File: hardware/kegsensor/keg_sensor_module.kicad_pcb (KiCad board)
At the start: 2 copper layers, 155 x 90 mm, 7 parts, among them J1 TerminalBlock_bornier-3_P5.08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, J2 TerminalBlock_bornier-3_P5.08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, J3 TerminalBlock_bornier-3_P5.08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, J4 TerminalBlock_bornier-3_P5.08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, J5 PinSocket_1x04_P2.54mm_Vertic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, J6 PinSocket_1x04_P2.54mm_Vertic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, J7 RJ14_Connfly_DS1133-S4_Horizo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

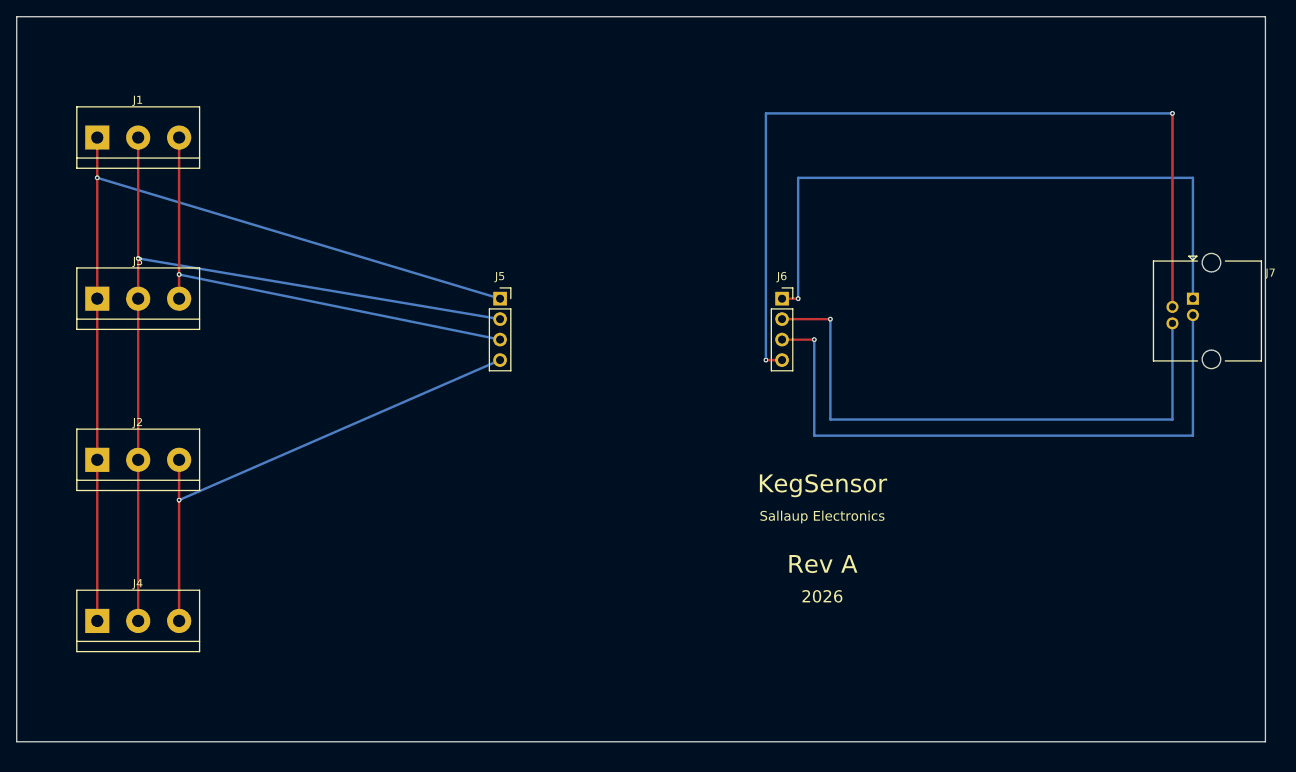
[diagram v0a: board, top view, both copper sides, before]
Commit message: Move KegSensor's J1-J4 sensor terminals to a horizontal row near the top edge
Previously a vertical column near the left edge. Rotated each terminal
block -90deg so its 3 pins stack in Y instead of spreading in X - without
that, all 4 parts' pins would land on identical y-values and the
EXC_POS/EXC_NEG/SIG_POS/SIG_NEG buses couldn't cross the row without
shorting. Rerouted the J1-J4<->J5 bus accordingly; went through a couple
of DRC-guided rounds after straight diagonals cut through unrelated pads
(J2's own pad, then J5's adjacent pad) and an existing J6<->J7 GND trace
that now ran too close to J4's new position.

Also fixed a latent bug the multi-instance footprint copies exposed:
generate_pcb.py kept each copied footprint's nested pad/graphic UUIDs
verbatim from the library file, so J1/J3/J2/J4 (all the same footprint)
shared identical pad UUIDs and confused DRC's violation reporting. Now
re-rolls every nested UUID per instance.

Case updated to match: the J1-J4 wire-exit cutout moved from the left
wall to the front wall, so the engraved branding (which lived there)
moved to the back wall instead, reusing the already-implemented
wall_text_back() - re-verified correct via a mirrored 2D cross-section
from the actual outside-viewer's perspective.

ERC clean, DRC 0 errors (only pre-existing accepted warnings remain),
both case STLs still Simple: yes.

Co-Authored-By: Claude Sonnet 5 <noreply@anthropic.com>
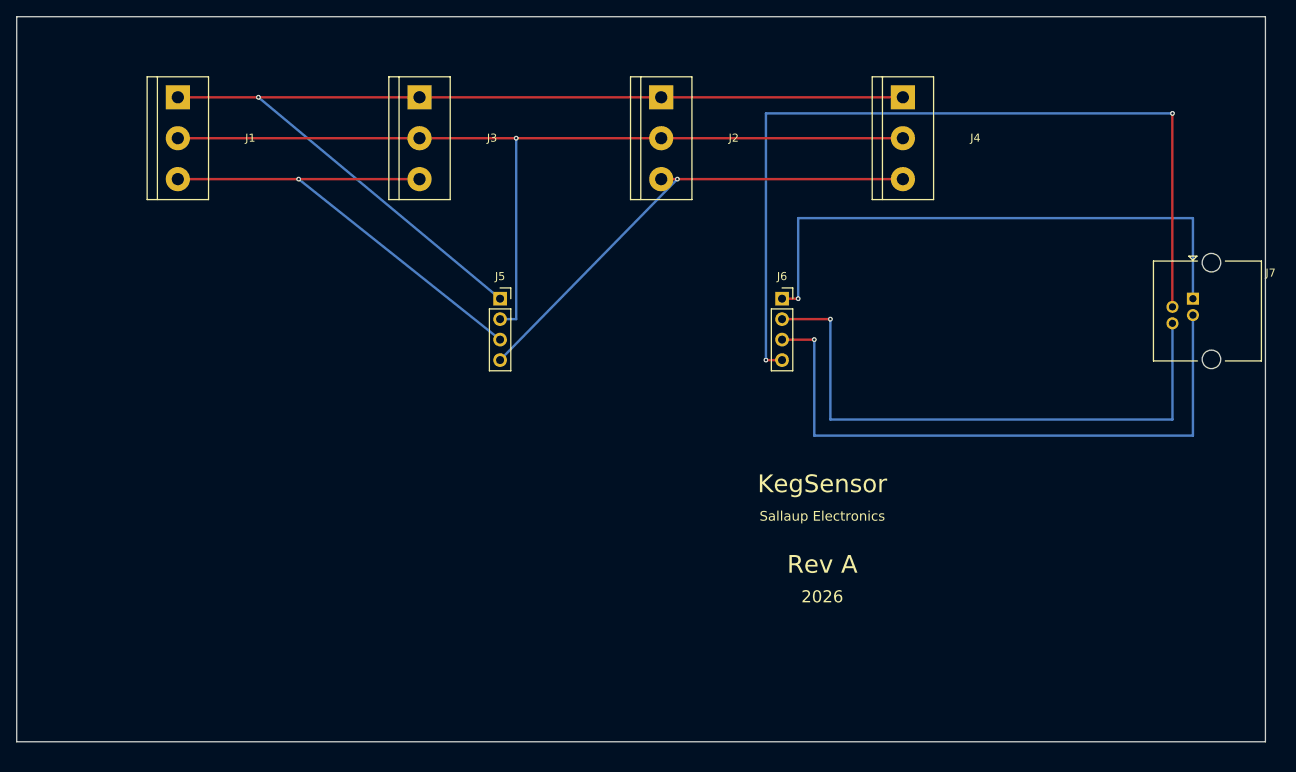
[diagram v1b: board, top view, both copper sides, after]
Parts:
- moved J4 119.3 mm to (110.0, 10.0), turned to -90 degrees
- moved J2 83.2 mm to (80.0, 10.0), turned to -90 degrees
- moved J3 47.2 mm to (50.0, 10.0), turned to -90 degrees
- moved J1 11.2 mm to (20.0, 10.0), turned to -90 degrees
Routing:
- net EXC_POS: track 112.2 -> 129.1 mm
- net GND: track 81.0 -> 71.0 mm
- net EXC_NEG: track 105.5 -> 114.5 mm
- net SIG_NEG: track 63.5 -> 61.4 mm
- net SIG_POS: track 60.7 -> 62.0 mm
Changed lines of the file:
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@@
 (footprint "TerminalBlock:TerminalBlock_bornier-3_P5.08mm"
 		(layer "F.Cu")
-		(at 10 15 0)
+		(at 20 10 -90)
 		(attr through_hole)
 	(version 20241229)
@@
 	(tags "terminal block bornier3")
 	(property "Reference" "J1"
-		(at 5.05 -4.65 0)
+		(at 5.05 -9 0)
 		(layer "F.SilkS")
 		(effects
@@
 (footprint "TerminalBlock:TerminalBlock_bornier-3_P5.08mm"
 		(layer "F.Cu")
-		(at 10 35 0)
+		(at 50 10 -90)
 		(attr through_hole)
 	(version 20241229)
@@
 	(tags "terminal block bornier3")
 	(property "Reference" "J3"
-		(at 5.05 -4.65 0)
+		(at 5.05 -9 0)
 		(layer "F.SilkS")
 		(effects
@@
 (footprint "TerminalBlock:TerminalBlock_bornier-3_P5.08mm"
 		(layer "F.Cu")
-		(at 10 55 0)
+		(at 80 10 -90)
 		(attr through_hole)
 	(version 20241229)
@@
 	(tags "terminal block bornier3")
 	(property "Reference" "J2"
-		(at 5.05 -4.65 0)
+		(at 5.05 -9 0)
 		(layer "F.SilkS")
 		(effects
@@
 (footprint "TerminalBlock:TerminalBlock_bornier-3_P5.08mm"
 		(layer "F.Cu")
-		(at 10 75 0)
+		(at 110 10 -90)
 		(attr through_hole)
 	(version 20241229)
@@
 	(tags "terminal block bornier3")
 	(property "Reference" "J4"
-		(at 5.05 -4.65 0)
+		(at 5.05 -9 0)
 		(layer "F.SilkS")
 		(effects
@@
 )
 	(segment
-		(start 10 15)
-		(end 10 75)
+		(start 20 10)
+		(end 110 10)
 		(width 0.3)
 		(layer "F.Cu")
@@
 	)
 	(segment
-		(start 10 20)
+		(start 30 10)
 		(end 60 35)
 		(width 0.3)
@@
 	)
 	(segment
-		(start 15.08 15)
-		(end 15.08 75)
+		(start 20 15.08)
+		(end 110 15.08)
 		(width 0.3)
 		(layer "F.Cu")
@@
 	)
 	(segment
-		(start 15.08 30)
-		(end 60 37.54)
+		(start 62 15.08)
+		(end 62 37.54)
 		(width 0.3)
 		(layer "B.Cu")
@@
 	)
 	(segment
-		(start 20.16 15)
-		(end 20.16 35)
+		(start 62 37.54)
+		(end 60 37.54)
+		(width 0.3)
+		(layer "B.Cu")
+		(net 2)
+	)
+	(segment
+		(start 20 20.16)
+		(end 50 20.16)
 		(width 0.3)
 		(layer "F.Cu")
@@
 	)
 	(segment
-		(start 20.16 32)
+		(start 35 20.16)
 		(end 60 40.08)
 		(width 0.3)
@@
 	)
 	(segment
-		(start 20.16 55)
-		(end 20.16 75)
+		(start 80 20.16)
+		(end 110 20.16)
 		(width 0.3)
 		(layer "F.Cu")
@@
 	)
 	(segment
-		(start 20.16 60)
+		(start 82 20.16)
 		(end 60 42.62)
 		(width 0.3)
@@
 	(segment
 		(start 97 35)
-		(end 97 20)
+		(end 97 25)
 		(width 0.3)
 		(layer "B.Cu")
@@
 	)
 	(segment
-		(start 97 20)
-		(end 146 20)
+		(start 97 25)
+		(end 146 25)
 		(width 0.3)
 		(layer "B.Cu")
@@
 	)
 	(segment
-		(start 146 20)
+		(start 146 25)
 		(end 146 35)
 		(width 0.3)
@@
 	)
 	(via
-		(at 10 20)
+		(at 30 10)
 		(size 0.6)
 		(drill 0.3)
@@
 	)
 	(via
-		(at 15.08 30)
+		(at 62 15.08)
 		(size 0.6)
 		(drill 0.3)
@@
 	)
 	(via
-		(at 20.16 32)
+		(at 35 20.16)
 		(size 0.6)
 		(drill 0.3)
@@
 	)
 	(via
-		(at 20.16 60)
+		(at 82 20.16)
 		(size 0.6)
 		(drill 0.3)

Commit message: Un-rotate J1-J4, move J7 to the bottom edge, redesign all routing
J1-J4 back to angle=0 (unrotated) per explicit request - loses the
trivial per-pin bus that rotation gave, so the row now needs dedicated
lanes with layer alternation (EXC_POS on F.Cu, EXC_NEG on B.Cu) and via
hops (SIG_POS/SIG_NEG, which must cross both) to reach J5 without
shorting.

J7 moved from the right edge to the bottom edge (angle=180, verified via
actual DRC-reported pad/courtyard coordinates rather than assumed). Its
GND/SCK/VCC/DT approaches from J6 are redesigned around the same tight
~1mm pad spacing as before, just transposed to the new geometry -
straight verticals into GND/SCK grazed the adjacent VCC pad, fixed with
offset approaches and a final short jog at each pad's own y, plus
depth-ordered lanes so a deeper net's horizontal run doesn't cross a
shallower net's drop.

Also fixed along the way: a straight diagonal from J1-J4's row cut
through the SIG_POS lane, and SIG_NEG's approach crossed straight through
the J6<->J7 corridor - both real DRC errors, not style. ERC clean, DRC 0
errors (1 pre-existing accepted warning).

Case updated to match: J1-J4's cutout stays on the front wall (widened
for the now-unrotated, wider courtyard), J7's cutout moves from the
right wall to the back wall, and branding moves to the right wall (the
one now-plain wall) via a new wall_text_right() module - derived from
scratch (a right wall isn't front/back with axes swapped) and verified
correct via a true 2D cross-section, same method as before.

Regenerated fab/ Gerbers, drill files, PCB renders, and schematic PDF to
match.

Co-Authored-By: Claude Sonnet 5 <noreply@anthropic.com>
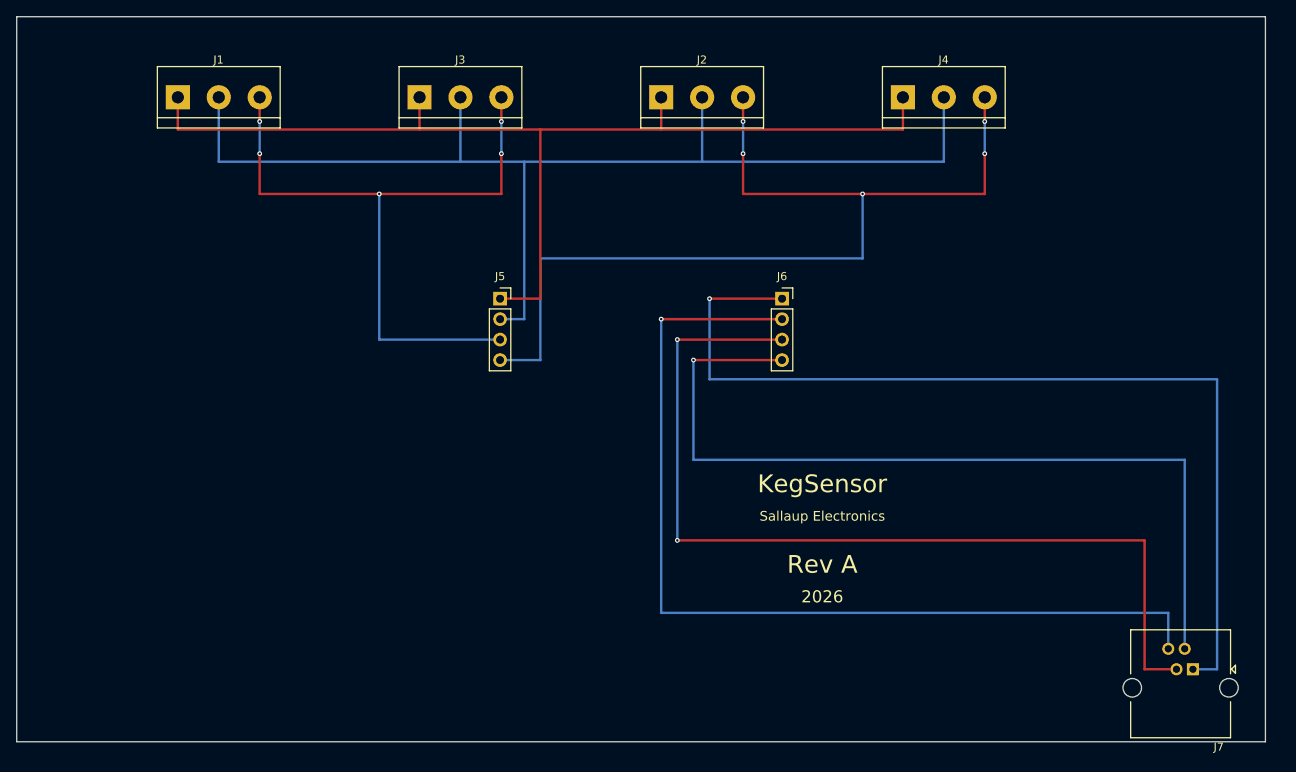
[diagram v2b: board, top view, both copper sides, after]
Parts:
- moved J7 46.0 mm to (146.0, 81.0), turned to 180 degrees
- turned J1 to 0 degrees
- turned J2 to 0 degrees
- turned J3 to 0 degrees
- turned J4 to 0 degrees
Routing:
- net SIG_NEG: track 61.4 -> 119.6 mm, vias 1 -> 5
- net GND: track 71.0 -> 121.0 mm
- net DT: track 72.9 -> 118.9 mm
- net SCK: track 77.9 -> 115.9 mm, vias 1 -> 2
- net EXC_NEG: track 114.5 -> 144.5 mm, vias 1 -> 0
- net SIG_POS: track 62.0 -> 87.1 mm, vias 1 -> 5
- net EXC_POS: track 129.1 -> 132.0 mm, vias 1 -> 0
- net VCC_3V3: track 107.1 -> 107.8 mm, vias 2 -> 1

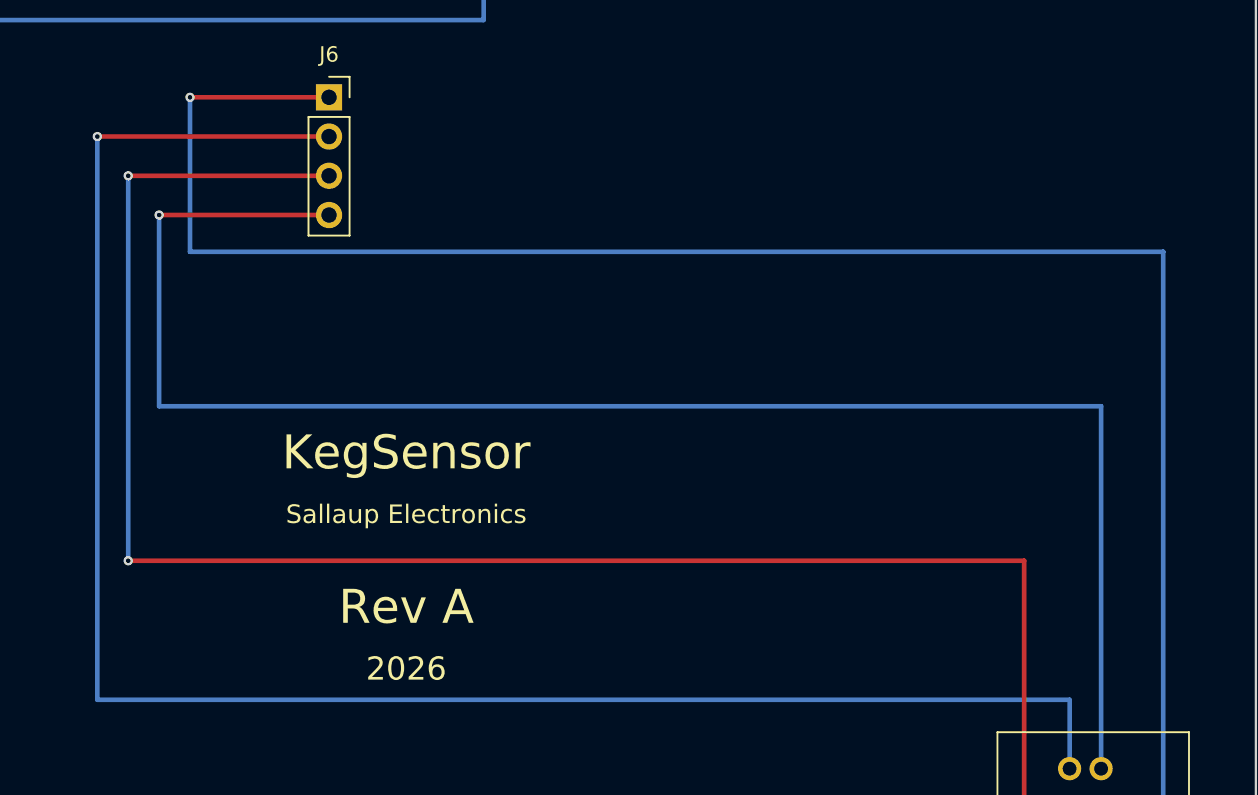
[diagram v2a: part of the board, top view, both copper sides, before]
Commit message: Route J6->J7 traces east first instead of west
Each net's initial jog off J6 now heads toward J7 (east) before turning
down to its lane, rather than doubling back west first. This flips
which net needs the shallowest lane: since every lane still extends the
rest of the way east to J7 regardless of where its own stub sits, the
depth/stub-position pairing that avoids crossings is the mirror image
of the west-jog version (shallowest lane <-> stub furthest from J6, not
closest). DRC clean on the first attempt with the reordered pairing.

Regenerated fab/ Gerbers, drill files, and PCB renders to match.

Co-Authored-By: Claude Sonnet 5 <noreply@anthropic.com>
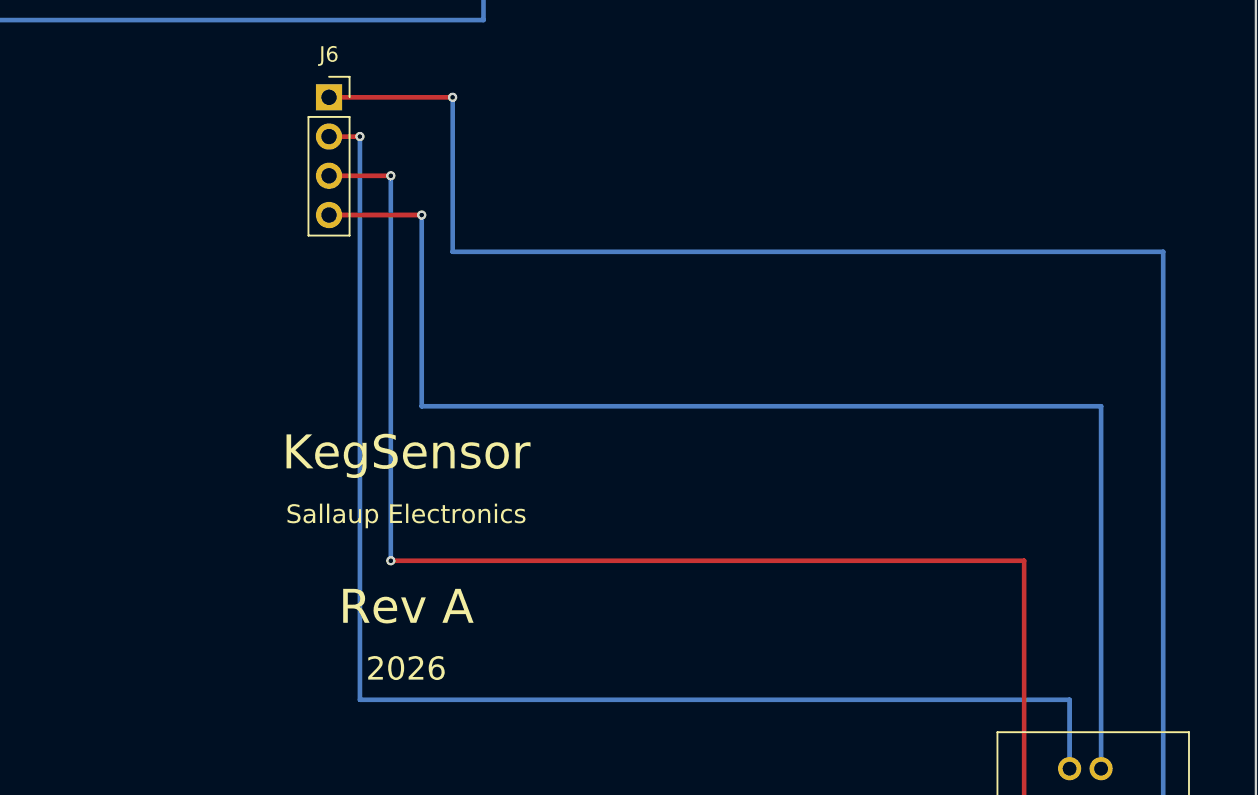
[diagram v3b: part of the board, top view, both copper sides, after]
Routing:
- net DT: track 118.9 -> 88.9 mm
- net SCK: track 115.9 -> 89.9 mm
- net VCC_3V3: track 107.8 -> 85.8 mm
- net GND: track 121.0 -> 103.0 mm
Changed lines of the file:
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@@
 	(segment
 		(start 95 35)
-		(end 86 35)
-		(width 0.3)
-		(layer "F.Cu")
-		(net 5)
-	)
-	(segment
-		(start 86 35)
-		(end 86 45)
-		(width 0.3)
-		(layer "B.Cu")
-		(net 5)
-	)
-	(segment
-		(start 86 45)
+		(end 103 35)
+		(width 0.3)
+		(layer "F.Cu")
+		(net 5)
+	)
+	(segment
+		(start 103 35)
+		(end 103 45)
+		(width 0.3)
+		(layer "B.Cu")
+		(net 5)
+	)
+	(segment
+		(start 103 45)
 		(end 149 45)
 		(width 0.3)
@@
 	(segment
 		(start 95 42.62)
-		(end 84 42.62)
-		(width 0.3)
-		(layer "F.Cu")
-		(net 8)
-	)
-	(segment
-		(start 84 42.62)
-		(end 84 55)
-		(width 0.3)
-		(layer "B.Cu")
-		(net 8)
-	)
-	(segment
-		(start 84 55)
+		(end 101 42.62)
+		(width 0.3)
+		(layer "F.Cu")
+		(net 8)
+	)
+	(segment
+		(start 101 42.62)
+		(end 101 55)
+		(width 0.3)
+		(layer "B.Cu")
+		(net 8)
+	)
+	(segment
+		(start 101 55)
 		(end 144.98 55)
 		(width 0.3)
@@
 	(segment
 		(start 95 40.08)
-		(end 82 40.08)
-		(width 0.3)
-		(layer "F.Cu")
-		(net 7)
-	)
-	(segment
-		(start 82 40.08)
-		(end 82 65)
-		(width 0.3)
-		(layer "B.Cu")
-		(net 7)
-	)
-	(segment
-		(start 82 65)
+		(end 99 40.08)
+		(width 0.3)
+		(layer "F.Cu")
+		(net 7)
+	)
+	(segment
+		(start 99 40.08)
+		(end 99 65)
+		(width 0.3)
+		(layer "B.Cu")
+		(net 7)
+	)
+	(segment
+		(start 99 65)
 		(end 140 65)
 		(width 0.3)
@@
 	(segment
 		(start 95 37.54)
-		(end 80 37.54)
-		(width 0.3)
-		(layer "F.Cu")
-		(net 6)
-	)
-	(segment
-		(start 80 37.54)
-		(end 80 74)
-		(width 0.3)
-		(layer "B.Cu")
-		(net 6)
-	)
-	(segment
-		(start 80 74)
+		(end 97 37.54)
+		(width 0.3)
+		(layer "F.Cu")
+		(net 6)
+	)
+	(segment
+		(start 97 37.54)
+		(end 97 74)
+		(width 0.3)
+		(layer "B.Cu")
+		(net 6)
+	)
+	(segment
+		(start 97 74)
 		(end 142.94 74)
 		(width 0.3)
@@
 	)
 	(via
-		(at 86 35)
-		(size 0.6)
-		(drill 0.3)
-		(layers "F.Cu" "B.Cu")
-		(net 5)
-	)
-	(via
-		(at 84 42.62)
-		(size 0.6)
-		(drill 0.3)
-		(layers "F.Cu" "B.Cu")
-		(net 8)
-	)
-	(via
-		(at 82 40.08)
-		(size 0.6)
-		(drill 0.3)
-		(layers "F.Cu" "B.Cu")
-		(net 7)
-	)
-	(via
-		(at 82 65)
-		(size 0.6)
-		(drill 0.3)
-		(layers "F.Cu" "B.Cu")
-		(net 7)
-	)
-	(via
-		(at 80 37.54)
-		(size 0.6)
-		(drill 0.3)
+		(at 103 35)
+		(size 0.6)
+		(drill 0.3)
+		(layers "F.Cu" "B.Cu")
+		(net 5)
+	)
+	(via
+		(at 101 42.62)
+		(size 0.6)
+		(drill 0.3)
+		(layers "F.Cu" "B.Cu")
+		(net 8)
+	)
+	(via
+		(at 99 40.08)
+		(size 0.6)
+		(drill 0.3)
+		(layers "F.Cu" "B.Cu")
+		(net 7)
+	)
+	(via
+		(at 99 65)
+		(size 0.6)
+		(drill 0.3)
+		(layers "F.Cu" "B.Cu")
+		(net 7)
+	)
+	(via
+		(at 97 37.54)
+		(size 0.6)
+		(drill 0.3)
